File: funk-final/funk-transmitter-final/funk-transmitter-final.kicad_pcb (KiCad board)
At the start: 2 copper layers, 41.9 x 41.3 mm, 7 parts, among them J1 Conn_01x02_Socket, J2 Conn_01x02_Socket, J4 Conn_01x05_Socket, J5 Conn_01x03_Socket, U1 Si4463_eigen

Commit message: ...
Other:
- board text removed: "ANT"
- board text removed: "GND"
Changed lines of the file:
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@@
     (pad_to_mask_clearance 0)
     (pcbplotparams
-      (layerselection 0x00010fc_ffffffff)
+      (layerselection 0x0001020_ffffffff)
       (plot_on_all_layers_selection 0x0000000_00000000)
       (disableapertmacros false)
@@
       (outputformat 1)
       (mirror false)
-      (drillshape 1)
+      (drillshape 0)
       (scaleselection 1)
-      (outputdirectory "")
+      (outputdirectory "../plot/")
     )
   )
@@
   (gr_rect (start 126.7 80.9) (end 168.6 122.2)
     (stroke (width 0.1) (type default)) (fill none) (layer "Edge.Cuts"))
-  (gr_text "ANT" (at 155.3 87.1) (layer "F.SilkS")
-    (effects (font (size 1 1) (thickness 0.15)) (justify left bottom))
-  )
   (gr_text "Funkmodul 4BHEL" (at 127.3 83.7) (layer "F.SilkS")
     (effects (font (size 1.5 1.5) (thickness 0.1875)) (justify left bottom))
   )
-  (gr_text "GPIO0" (at 157 101.4) (layer "F.SilkS")
+  (gr_text "GPIO0" (at 157.2 100.2) (layer "F.SilkS")
     (effects (font (size 1 1) (thickness 0.15)) (justify left bottom))
   )
-  (gr_text "GPIO1" (at 157.1 98.8) (layer "F.SilkS")
+  (gr_text "GPIO1" (at 157.2 97.7) (layer "F.SilkS")
     (effects (font (size 1 1) (thickness 0.15)) (justify left bottom))
   )
-  (gr_text "GND" (at 155.3 90.1) (layer "F.SilkS")
+  (gr_text "nIRQ" (at 157.4 102.6) (layer "F.SilkS")
     (effects (font (size 1 1) (thickness 0.15)) (justify left bottom))
   )
-  (gr_text "nIRQ" (at 157.2 103.8) (layer "F.SilkS")
-    (effects (font (size 1 1) (thickness 0.15)) (justify left bottom))
-  )

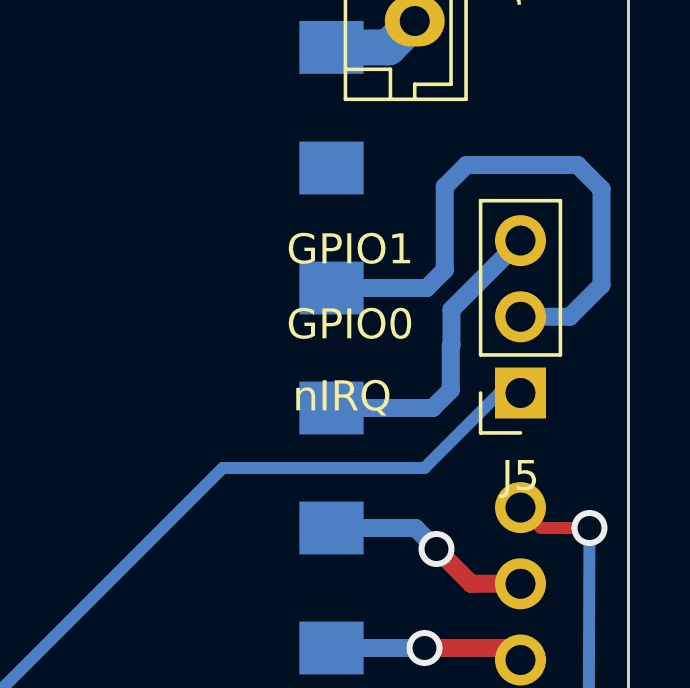
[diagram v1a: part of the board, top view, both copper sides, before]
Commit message: display and funk changed
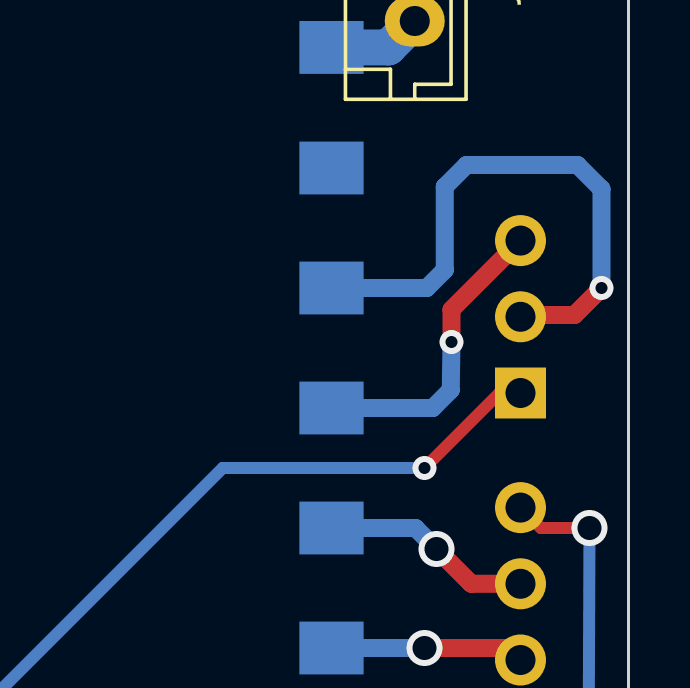
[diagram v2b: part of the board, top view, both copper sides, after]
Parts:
- J5: footprint Connector_PinSocket_2.54mm:PinSocket_1x03_P2.54mm_Vertical -> Connector_PinHeader_2.54mm:PinHeader_1x03_P2.54mm_Vertical; moved to B.Cu
- turned J5 to 0 degrees
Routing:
- net /nIRQ: track 56.3 -> 57.0 mm, vias 0 -> 1
- net /GPIO0: track 18.8 -> 19.0 mm, vias 0 -> 1
- net /GPIO1: track 9.99 -> 10.1 mm, vias 0 -> 1
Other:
- board text removed: "GPIO0"
- board text removed: "GPIO1"
- board text removed: "nIRQ"

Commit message: platinen angepasst
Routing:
- added copper zone on In1.Cu, net GND
- added copper zone on In2.Cu, net GND
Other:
- copper layers 2 -> 4
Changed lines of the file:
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@@
   (layers
     (0 "F.Cu" signal)
+    (1 "In1.Cu" signal)
+    (2 "In2.Cu" signal)
     (31 "B.Cu" signal)
     (32 "B.Adhes" user "B.Adhesive")
@@
       (layer "F.Mask" (type "Top Solder Mask") (thickness 0.01))
       (layer "F.Cu" (type "copper") (thickness 0.035))
-      (layer "dielectric 1" (type "core") (thickness 1.51) (material "FR4") (epsilon_r 4.5) (loss_tangent 0.02))
+      (layer "dielectric 1" (type "prepreg") (thickness 0.1) (material "FR4") (epsilon_r 4.5) (loss_tangent 0.02))
+      (layer "In1.Cu" (type "copper") (thickness 0.035))
+      (layer "dielectric 2" (type "core") (thickness 1.24) (material "FR4") (epsilon_r 4.5) (loss_tangent 0.02))
+      (layer "In2.Cu" (type "copper") (thickness 0.035))
+      (layer "dielectric 3" (type "prepreg") (thickness 0.1) (material "FR4") (epsilon_r 4.5) (loss_tangent 0.02))
       (layer "B.Cu" (type "copper") (thickness 0.035))
       (layer "B.Mask" (type "Bottom Solder Mask") (thickness 0.01))
@@
     (polygon
       (pts
+        (xy 126.7 80.9)
+        (xy 168.6 80.9)
+        (xy 168.6 122.2)
+        (xy 126.7 122.2)
+      )
+    )
+  )
+  (zone (net 2) (net_name "GND") (layers "In1.Cu" "In2.Cu") (hatch edge 0.5)
+    (priority 2)
+    (connect_pads (clearance 0.5))
+    (min_thickness 0.25) (filled_areas_thickness no)
+    (fill yes (thermal_gap 0.5) (thermal_bridge_width 0.5))
+    (polygon
+      (pts
